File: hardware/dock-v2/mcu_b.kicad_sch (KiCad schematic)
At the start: 0 parts

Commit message: Dock v2: all parts placed on their sheets (not wired)
149 parts across POWER, USB_PORTS, MCU_A, MCU_B, BLE and POGO (A3), in
labelled groups, with references (sheet x 100), values, footprints, LCSC
numbers (hidden LCSC field) and a Note per part. Only unconnected-pin ERC
messages remain.

5 V buck values from TI's TPS54331 Table 7-1 (5 V design), moved to Basic
parts: 12k/2.2k feedback (5.16 V), 51k + 4.7nF + 47pF compensation, 10 nF
soft start, 3 x 22 uF out; recorded in docs/dock-v2-power-input.md.
New footprint dock_v2:CP_Radial_D6.3mm_P5.00mm for the hand-soldered 220 uF.

Co-Authored-By: Claude Opus 5.5 <noreply@anthropic.com>
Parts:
- added C401, C402: 4.7uF, dock_v2:C_0402_RPi_Wide, symbol Device:C
- added C403: 4.7uF, Capacitor_SMD:C_0402_1005Metric, symbol Device:C
- added C404, C405, C406, C407, C408, C409, C410, C411, C412, C413: 100nF, Capacitor_SMD:C_0402_1005Metric, symbol Device:C
- added C414: 10uF, Capacitor_SMD:C_0805_2012Metric, symbol Device:C
- added C415, C416: 15pF, Capacitor_SMD:C_0402_1005Metric, symbol Device:C
- added D401: LED red, LED_SMD:LED_0603_1608Metric, symbol Device:LED
- added L401: 3.3uH, dock_v2:L_Abracon_AOTA-B201610S3R3_0806, symbol Device:L
- added R401: 33, Resistor_SMD:R_0402_1005Metric, symbol Device:R
- added R402, R403, R404, R405: 1k, Resistor_SMD:R_0402_1005Metric, symbol Device:R
- added SW401: SW_Push, Button_Switch_SMD:SW_Push_1P1T_XKB_TS-1187A, symbol Switch:SW_Push
- added TP401, TP402, TP403: TestPoint, TestPoint:TestPoint_Pad_D1.0mm, symbol Connector:TestPoint
- added U401: RP2354A, dock_v2:RP2350A_QFN-60_RPi_Vias, symbol dock_v2_custom:RP2354A_RPiFP
- added Y401: 12MHz, Crystal:Crystal_SMD_3225-4Pin_3.2x2.5mm, symbol Device:Crystal_GND24
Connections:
- new net: U401.1 (IOVDD), U401.11 (IOVDD), U401.20 (IOVDD), U401.30 (IOVDD), U401.38 (IOVDD), U401.45 (IOVDD)
- new net: U401.23 (DVDD), U401.39 (DVDD), U401.6 (DVDD)
- new net: Y401.2 (G), Y401.4 (G)
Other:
- note added: "Buttons, SWD pads, LED"
- note added: "Core regulator (copy_rpi_core_layout.py)"
- note added: "Crystal"
- note added: "Decoupling"
- note added: "RP2354A B"

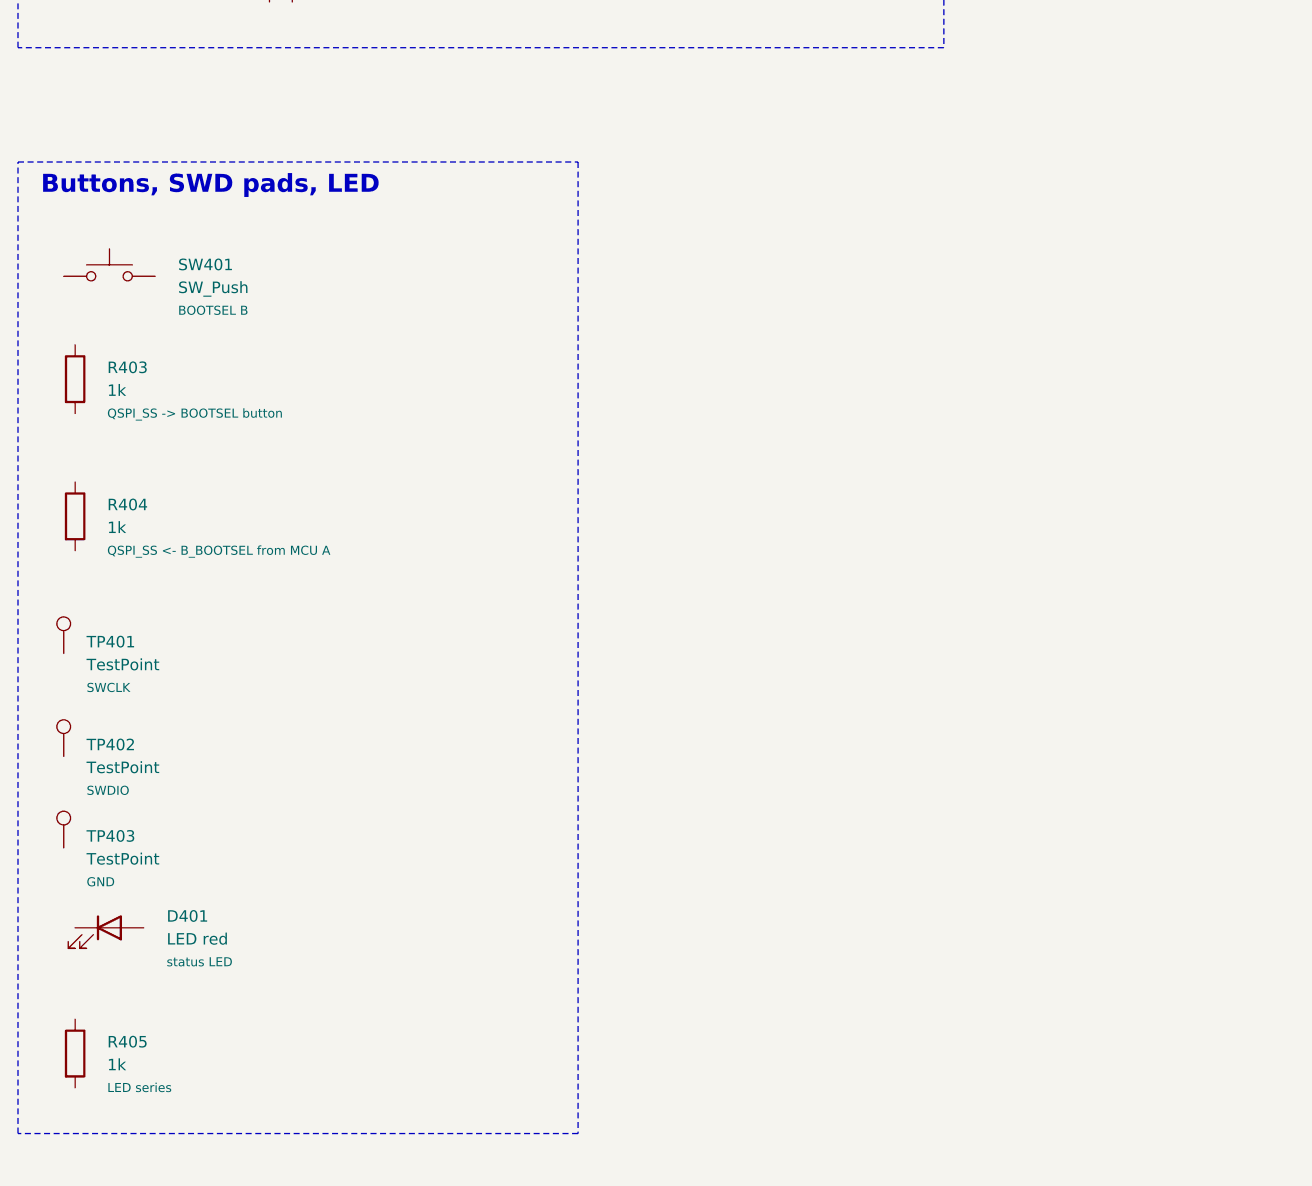
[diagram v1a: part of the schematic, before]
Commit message: Dock v2: connection guide (DOCK_CONNECTIONS.md), pin maps, wiring checker
hardware/dock-v2/DOCK_CONNECTIONS.md, in the style of the pad's guide: per
sheet a sketch, parts table (value, footprint, LCSC, job), pin-by-pin wiring
tables, placement notes; MCU A/B pin maps; nets that cross sheets (global
labels); PWR_FLAG and no-connect lists; full net index. Tables are generated
from one connection model (tools/dock_v2_connections/dock_nets.py) that is
checked against the placed schematic: 570 pins, each on a net or NC exactly once.

Found while making the pin map: MCU A's pins are weak pull-downs at reset, so
added 10k pull-ups on B_RUN, B_BOOTSEL (R406, R407) and ESP32 GPIO9 (R504),
and POGO_OFF now drives its own 2N7002 (Q602, R609) so a blank MCU A can't
switch off pad charging. 154 parts.

tools/dock_v2_connections/check_wiring.py compares the wired schematic with
the guide (unwired / split / merged / NC); make_doc.py regenerates the guide.

Co-Authored-By: Claude Opus 5.5 <noreply@anthropic.com>
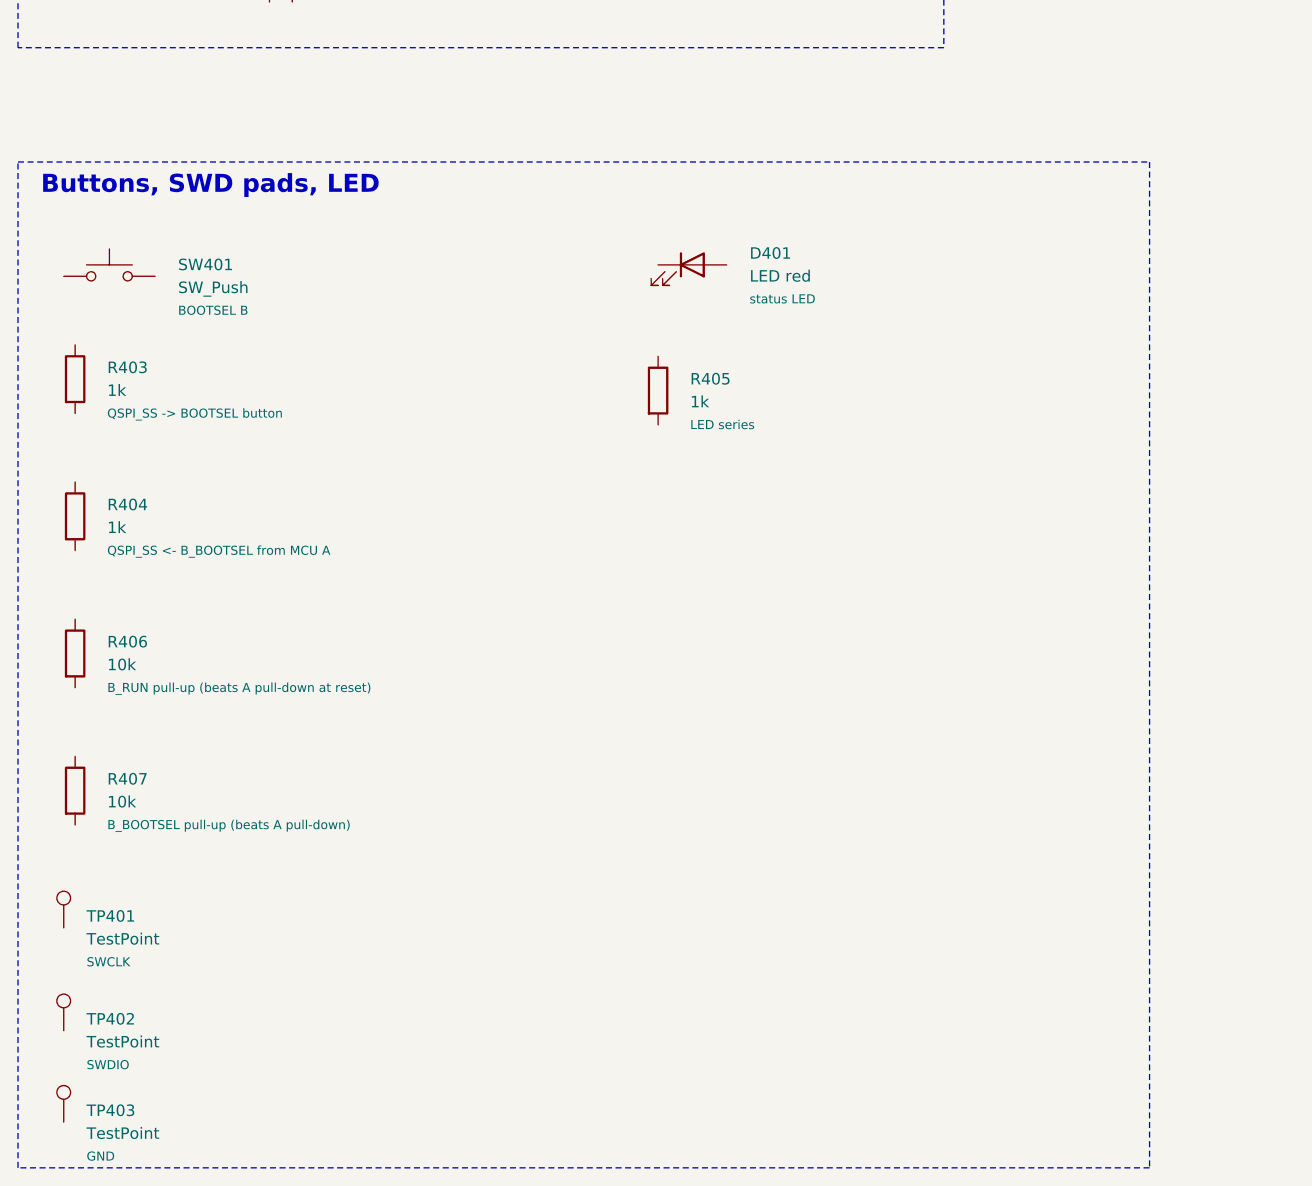
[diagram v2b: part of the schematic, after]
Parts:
- added R406, R407: 10k, Resistor_SMD:R_0402_1005Metric, symbol Device:R
